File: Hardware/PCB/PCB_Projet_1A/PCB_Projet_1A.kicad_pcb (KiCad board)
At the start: 4 copper layers, 46.5 x 64 mm, 42 parts, among them J1 Conn_01x03, J10 Conn_01x02, J11 BU33SD5WG-TR, J12 R-78B5.0-2.0, J2 Conn_01x04, J3 Conn_01x03, J4 Conn_01x04, J5 Conn_01x04, J6 Conn_ST_STDC14, J7 Conn_01x04, J8 Conn_01x02, J9 Conn_01x02, U1 HC-05, U2 STM32L552CCTx

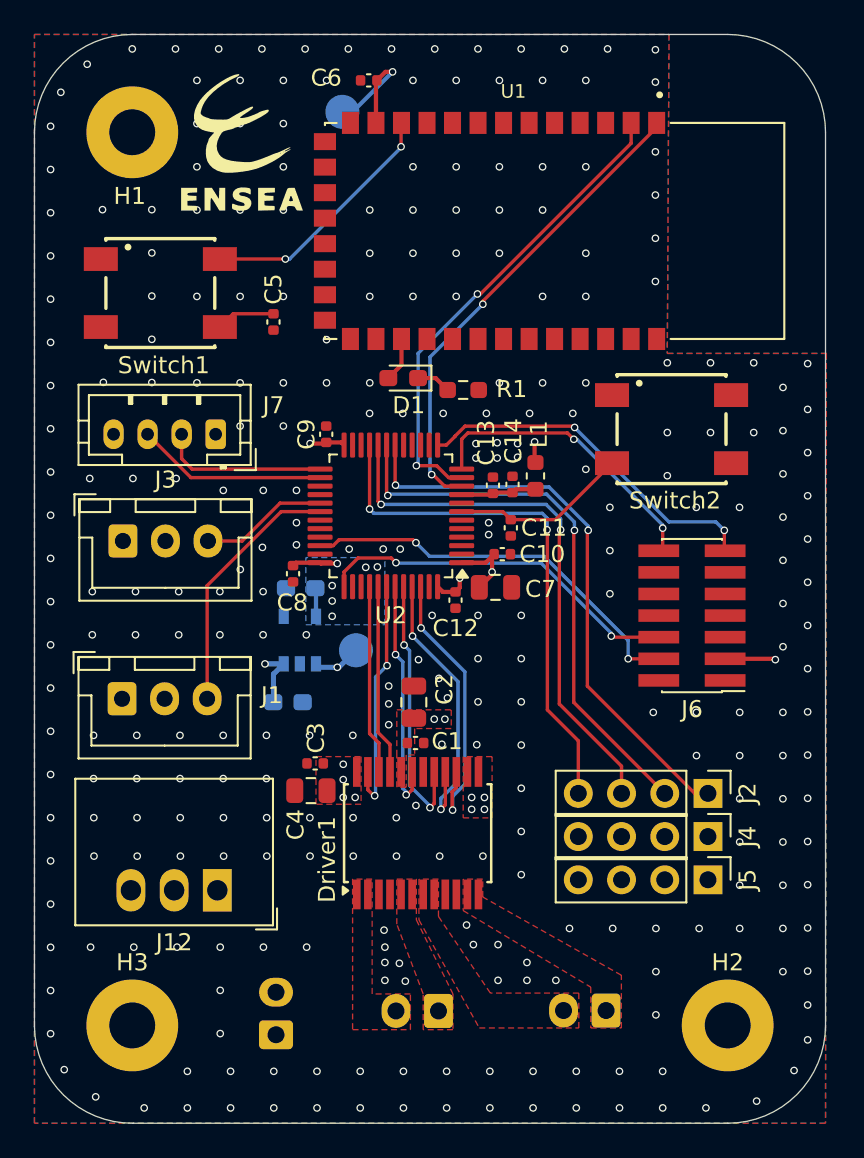
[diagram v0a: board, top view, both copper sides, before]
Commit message: Modification du PCB: changement du HC05 SMD en pinheader adapté au module
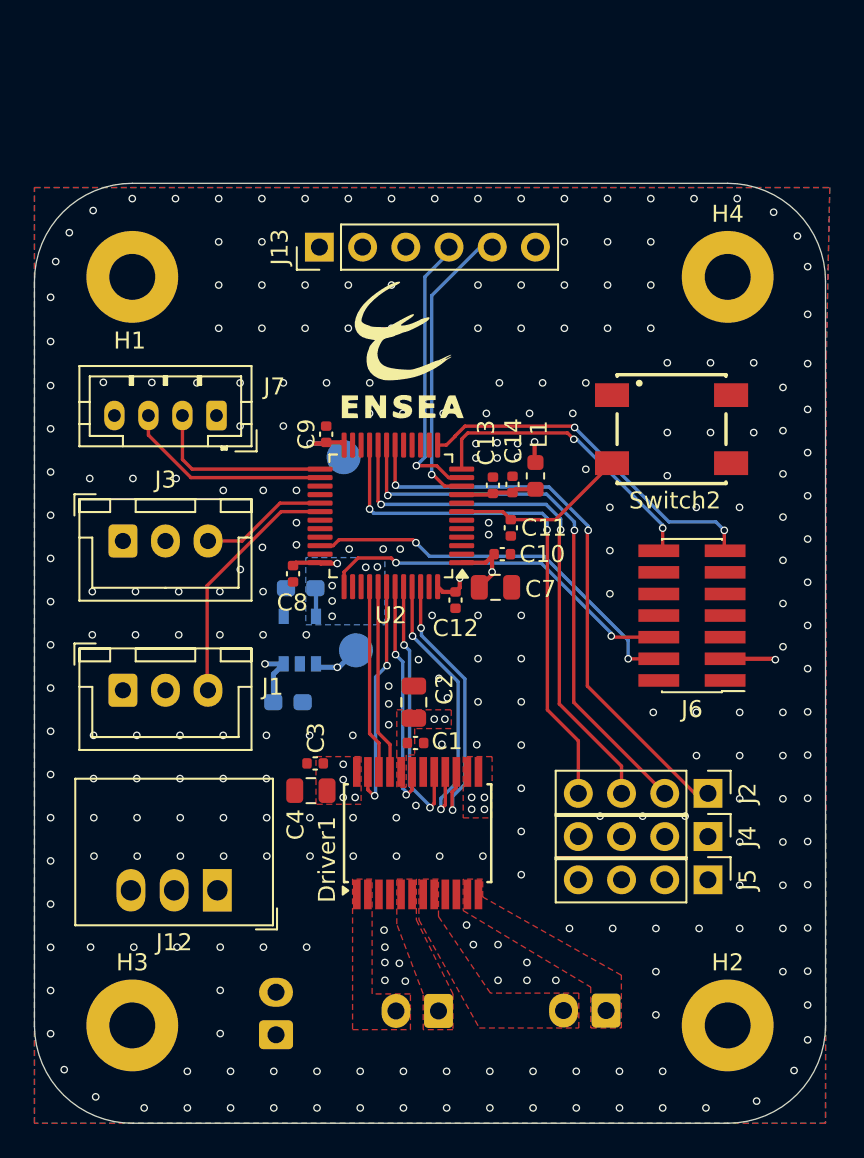
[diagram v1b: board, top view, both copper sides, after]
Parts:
- removed C5, C6: 100n, Capacitor_SMD:C_0402_1005Metric
- removed D1: LED, LED_SMD:LED_0603_1608Metric_Pad1.05x0.95mm_HandSolder
- removed R1: 1k, Resistor_SMD:R_0603_1608Metric_Pad0.98x0.95mm_HandSolder
- removed Switch1: 430471025826, boutonSMD_wurth430471025826:430471025826
- removed U1: HC-05, HC-05:XCVR_HC-05
- added H4: MountingHole_Pad, MountingHole:MountingHole_2.7mm_M2.5_Pad, F.Cu at (181.0, 65.0)
- added J13: Conn_01x06, Connector_PinHeader_2.54mm:PinHeader_1x06_P2.54mm_Vertical, F.Cu at (157.0, 63.2)
- moved TP2 20.3 mm to (158.4, 75.6)
- moved G*** 15.4 mm to (161.9, 69.6)
- moved H1 8.50 mm to (146.0, 65.0)
- moved J7 1.10 mm to (150.9, 73.2)
- moved J1 0.50 mm to (145.4, 89.3)
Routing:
- net Net-(U1-~{RESETB}): track 14.8 -> 0.00 mm, vias 2 -> 0
- net UART4_RX: track 28.4 -> 16.6 mm, vias 2 -> 1
- net UART4_TX: track 28.3 -> 17.3 mm, vias 2 -> 1
- net +3.3V: track 24.8 -> 19.5 mm, vias 14 -> 13
- net Net-(C5-Pad2): track 3.47 -> 0.00 mm
- net Net-(D1-A): track 2.62 -> 0.00 mm
- net Net-(D1-K): track 2.03 -> 0.00 mm
- net Echo: track 11.2 -> 12.3 mm
- net Triger: track 9.83 -> 10.9 mm
- net GND: vias 299 -> 278
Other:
- board size 46.5 x 64 mm -> 46.5 x 55.2 mm

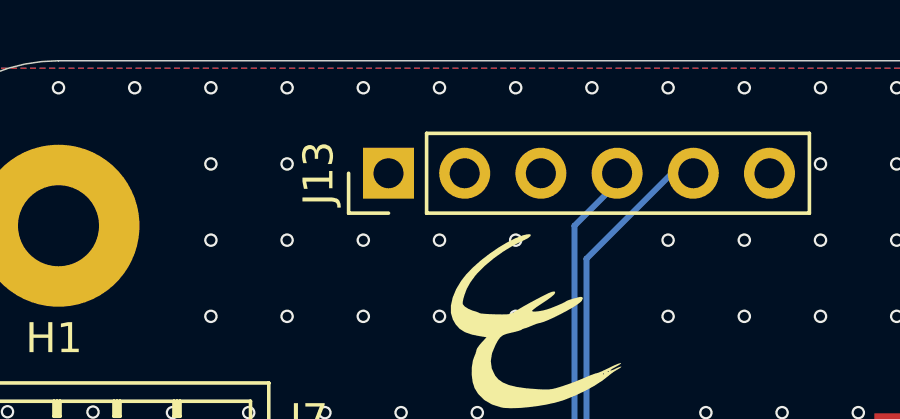
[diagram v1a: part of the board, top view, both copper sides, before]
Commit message: modification de F.silkscreen et B.silkscreen et du README PCB
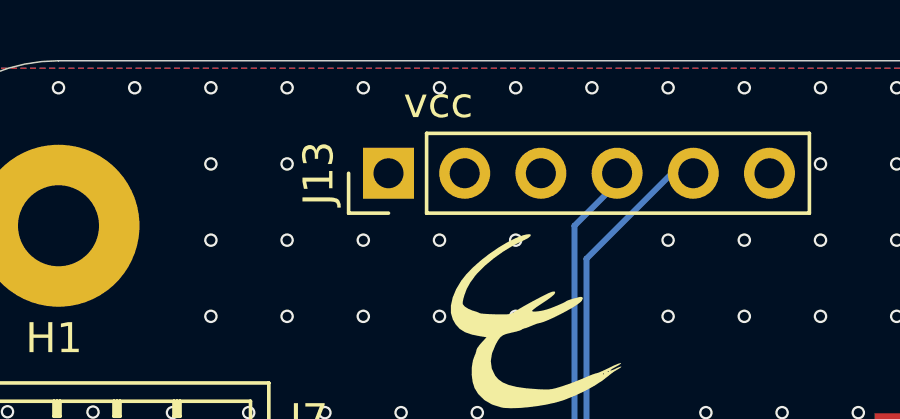
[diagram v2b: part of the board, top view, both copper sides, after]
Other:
- board text added: "uart4_rx"
- board text added: "uart4_tx"
- board text added: "vcc"
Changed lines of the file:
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@@
 		)
 		(fp_text user "${REFERENCE}"
-			(at 0 6.35 360)
+			(at 0 6.35 0)
 			(layer "F.Fab")
 			(effects
@@
 		(layer "Edge.Cuts")
 	)
+	(gr_text "uart4_tx"
+		(at 166.8 70.5 270)
+		(layer "B.SilkS")
+		(effects
+			(font
+				(size 1 1)
+				(thickness 0.1)
+			)
+			(justify left bottom mirror)
+		)
+	)
+	(gr_text "uart4_rx"
+		(at 164 70.5 -90)
+		(layer "B.SilkS")
+		(effects
+			(font
+				(size 1 1)
+				(thickness 0.1)
+			)
+			(justify left bottom mirror)
+		)
+	)
 	(gr_text "PCB Projet 1A\nCapodagli Janus\nBui Hai Christophe\nMillon Raphaelle"
 		(at 183 86.5 0)
@@
 		)
 	)
+	(gr_text "vcc"
+		(at 159 67 -90)
+		(layer "B.SilkS")
+		(effects
+			(font
+				(size 1 1)
+				(thickness 0.1)
+			)
+			(justify left bottom mirror)
+		)
+	)
+	(gr_text "vcc"
+		(at 157.5 61.5 0)
+		(layer "F.SilkS")
+		(effects
+			(font
+				(size 1 1)
+				(thickness 0.1)
+			)
+			(justify left bottom)
+		)
+	)
 	(via
 		(at 153.8 87.75)
@@
 			(pts
 				(xy 153.475 69.8) (xy 153.525 71.6) (xy 153.55 70.85) (xy 153.55 86.1) (xy 159.1 86.1) (xy 159.1 93.05)
-				(xy 168.65 93.1) (xy 168.75 114.2) (xy 186.3 114.2) (xy 186.25 69.5) (xy 177.5 69.45) (xy 177.5 69.45)
+				(xy 168.65 93.1) (xy 168.75 114.2) (xy 186.3 114.2) (xy 186.25 69.5) (xy 177.5 69.45)
 			)
 		)

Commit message: modif pcb
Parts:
- removed J4, J5: Conn_01x04, Connector_PinHeader_2.54mm:PinHeader_1x04_P2.54mm_Vertical
- added J14: Conn_01x03, Connector_PinHeader_2.54mm:PinHeader_1x03_P2.54mm_Vertical, F.Cu at (180.0, 94.9)
- added J15: Conn_01x03, Connector_PinHeader_2.54mm:PinHeader_1x03_P2.54mm_Vertical, F.Cu at (180.0, 100.0)
- added J16: Conn_01x03, Connector_PinHeader_2.54mm:PinHeader_1x03_P2.54mm_Vertical, F.Cu at (180.0, 97.5)
- J2: value Conn_01x04 -> Conn_01x02; footprint Connector_PinHeader_2.54mm:PinHeader_1x04_P2.54mm_Vertical -> Connector_PinHeader_2.54mm:PinHeader_1x02_P2.54mm_Horizontal; moved to B.Cu
- moved J2 30.7 mm to (161.5, 70.7), turned to 0 degrees
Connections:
- J2 pad 1: GPIO1 -> UART3_TX
- J2 pad 2: GPIO2 -> UART3_RX
- U2 pad 21: GPIO4 -> UART3_TX
- U2 pad 22: unconnected-(U2-PB11-Pad22) -> UART3_RX
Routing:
- net GPIO4: track 31.4 -> 0.00 mm, vias 2 -> 0
- net UART3_TX: track 0.00 -> 20.6 mm, vias 0 -> 2
- net UART3_RX: track 0.00 -> 7.63 mm
- net GND: vias 278 -> 276
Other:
- board text added: "RX"
- board text added: "TX"
- board text removed: "uart4_rx"
- board text removed: "uart4_tx"
